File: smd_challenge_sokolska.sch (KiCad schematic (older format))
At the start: 13 parts, among them U01 usb_supply

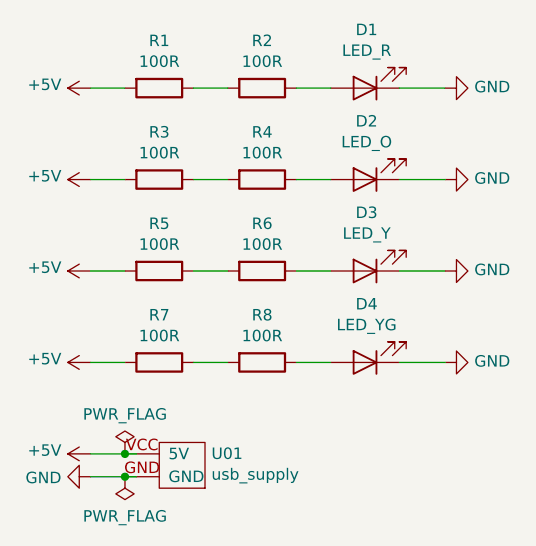
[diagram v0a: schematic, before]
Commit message: fixed part U01
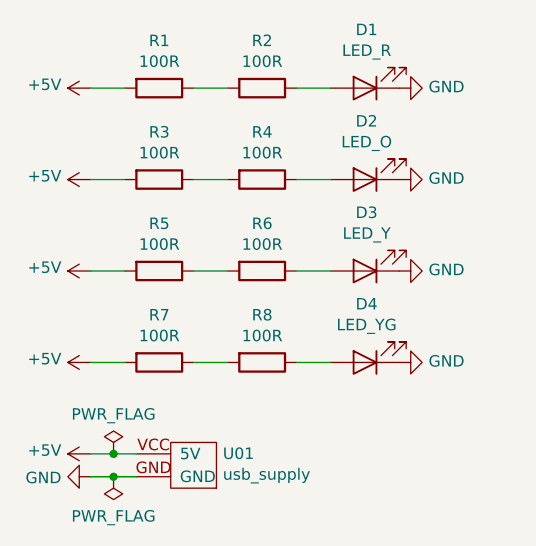
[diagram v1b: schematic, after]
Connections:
- wire segments 20 -> 16
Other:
- moved on the sheet: U01
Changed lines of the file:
@@
 Wire Wire Line
 	3350 3500 3500 3500
-$Comp
-L power:+5V #PWR01
-U 1 1 5FB98398
-P 2450 2300
-F 0 "#PWR01" H 2450 2150 50  0001 C CNN
-F 1 "+5V" V 2465 2428 50  0000 L CNN
-F 2 "" H 2450 2300 50  0001 C CNN
-F 3 "" H 2450 2300 50  0001 C CNN
-	1    2450 2300
-	0    -1   -1   0
-$EndComp
-$Comp
-L power:+5V #PWR03
-U 1 1 5FB98FA5
-P 2450 2700
-F 0 "#PWR03" H 2450 2550 50  0001 C CNN
-F 1 "+5V" V 2465 2828 50  0000 L CNN
-F 2 "" H 2450 2700 50  0001 C CNN
-F 3 "" H 2450 2700 50  0001 C CNN
-	1    2450 2700
-	0    -1   -1   0
-$EndComp
-$Comp
-L power:+5V #PWR05
-U 1 1 5FB993D5
-P 2450 3100
-F 0 "#PWR05" H 2450 2950 50  0001 C CNN
-F 1 "+5V" V 2465 3228 50  0000 L CNN
-F 2 "" H 2450 3100 50  0001 C CNN
-F 3 "" H 2450 3100 50  0001 C CNN
-	1    2450 3100
-	0    -1   -1   0
-$EndComp
-$Comp
-L power:+5V #PWR07
-U 1 1 5FB9982B
-P 2450 3500
-F 0 "#PWR07" H 2450 3350 50  0001 C CNN
-F 1 "+5V" V 2465 3628 50  0000 L CNN
-F 2 "" H 2450 3500 50  0001 C CNN
-F 3 "" H 2450 3500 50  0001 C CNN
-	1    2450 3500
-	0    -1   -1   0
-$EndComp
-$Comp
-L power:GND #PWR02
-U 1 1 5FB99BAF
-P 4000 2300
-F 0 "#PWR02" H 4000 2050 50  0001 C CNN
-F 1 "GND" V 4005 2172 50  0000 R CNN
-F 2 "" H 4000 2300 50  0001 C CNN
-F 3 "" H 4000 2300 50  0001 C CNN
-	1    4000 2300
-	0    -1   -1   0
-$EndComp
-$Comp
-L power:GND #PWR04
-U 1 1 5FB9A1E2
-P 4000 2700
-F 0 "#PWR04" H 4000 2450 50  0001 C CNN
-F 1 "GND" V 4005 2572 50  0000 R CNN
-F 2 "" H 4000 2700 50  0001 C CNN
-F 3 "" H 4000 2700 50  0001 C CNN
-	1    4000 2700
-	0    -1   -1   0
-$EndComp
-$Comp
-L power:GND #PWR06
-U 1 1 5FB9A544
-P 4000 3100
-F 0 "#PWR06" H 4000 2850 50  0001 C CNN
-F 1 "GND" V 4005 2972 50  0000 R CNN
-F 2 "" H 4000 3100 50  0001 C CNN
-F 3 "" H 4000 3100 50  0001 C CNN
-	1    4000 3100
-	0    -1   -1   0
-$EndComp
-$Comp
-L power:GND #PWR08
-U 1 1 5FB9A853
-P 4000 3500
-F 0 "#PWR08" H 4000 3250 50  0001 C CNN
-F 1 "GND" V 4005 3372 50  0000 R CNN
-F 2 "" H 4000 3500 50  0001 C CNN
-F 3 "" H 4000 3500 50  0001 C CNN
-	1    4000 3500
-	0    -1   -1   0
-$EndComp
 Wire Wire Line
 	2450 2300 2600 2300
@@
 Wire Wire Line
 	2450 3500 2600 3500
-Wire Wire Line
-	3800 3500 4000 3500
-Wire Wire Line
-	3800 3100 4000 3100
-Wire Wire Line
-	3800 2700 4000 2700
-Wire Wire Line
-	3800 2300 4000 2300
 $Comp
-L power:+5V #PWR09
-U 1 1 5FB9EA27
+L lib_smd_challenge:usb_supply U01
+U 1 1 5FBA6898
+P 2900 3950
+F 0 "U01" H 3028 4001 50  0000 L CNN
+F 1 "usb_supply" H 3028 3910 50  0000 L CNN
+F 2 "smd_challenge_sokolska:usb_supply" H 2700 4150 50  0001 C CNN
+F 3 "" H 2700 4150 50  0001 C CNN
+	1    2900 3950
+	1    0    0    -1
+$EndComp
+$Comp
+L power:+5V #PWR?
+U 1 1 5FBAC758
+P 2450 2300
+F 0 "#PWR?" H 2450 2150 50  0001 C CNN
+F 1 "+5V" V 2465 2428 50  0000 L CNN
+F 2 "" H 2450 2300 50  0001 C CNN
+F 3 "" H 2450 2300 50  0001 C CNN
+	1    2450 2300
+	0    -1   -1   0
+$EndComp
+$Comp
+L power:+5V #PWR?
+U 1 1 5FBACDBB
+P 2450 2700
+F 0 "#PWR?" H 2450 2550 50  0001 C CNN
+F 1 "+5V" V 2465 2828 50  0000 L CNN
+F 2 "" H 2450 2700 50  0001 C CNN
+F 3 "" H 2450 2700 50  0001 C CNN
+	1    2450 2700
+	0    -1   -1   0
+$EndComp
+$Comp
+L power:+5V #PWR?
+U 1 1 5FBAD238
+P 2450 3100
+F 0 "#PWR?" H 2450 2950 50  0001 C CNN
+F 1 "+5V" V 2465 3228 50  0000 L CNN
+F 2 "" H 2450 3100 50  0001 C CNN
+F 3 "" H 2450 3100 50  0001 C CNN
+	1    2450 3100
+	0    -1   -1   0
+$EndComp
+$Comp
+L power:+5V #PWR?
+U 1 1 5FBAD7C1
+P 2450 3500
+F 0 "#PWR?" H 2450 3350 50  0001 C CNN
+F 1 "+5V" V 2465 3628 50  0000 L CNN
+F 2 "" H 2450 3500 50  0001 C CNN
+F 3 "" H 2450 3500 50  0001 C CNN
+	1    2450 3500
+	0    -1   -1   0
+$EndComp
+$Comp
+L power:+5V #PWR?
+U 1 1 5FBADA85
 P 2450 3900
-F 0 "#PWR09" H 2450 3750 50  0001 C CNN
+F 0 "#PWR?" H 2450 3750 50  0001 C CNN
 F 1 "+5V" V 2465 4028 50  0000 L CNN
 F 2 "" H 2450 3900 50  0001 C CNN
@@
 $EndComp
 $Comp
-L power:GND #PWR010
-U 1 1 5FB9EDFF
+L power:GND #PWR?
+U 1 1 5FBAE10E
 P 2450 4000
-F 0 "#PWR010" H 2450 3750 50  0001 C CNN
+F 0 "#PWR?" H 2450 3750 50  0001 C CNN
 F 1 "GND" V 2455 3872 50  0000 R CNN
 F 2 "" H 2450 4000 50  0001 C CNN
@@
 	0    1    1    0
 $EndComp
+$Comp
+L power:GND #PWR?
+U 1 1 5FBAE6FF
+P 3800 2300
+F 0 "#PWR?" H 3800 2050 50  0001 C CNN
+F 1 "GND" V 3805 2172 50  0000 R CNN
+F 2 "" H 3800 2300 50  0001 C CNN
+F 3 "" H 3800 2300 50  0001 C CNN
+	1    3800 2300
+	0    -1   -1   0
+$EndComp
+$Comp
+L power:GND #PWR?
+U 1 1 5FBAFB2D
+P 3800 2700
+F 0 "#PWR?" H 3800 2450 50  0001 C CNN
+F 1 "GND" V 3805 2572 50  0000 R CNN
+F 2 "" H 3800 2700 50  0001 C CNN
+F 3 "" H 3800 2700 50  0001 C CNN
+	1    3800 2700
+	0    -1   -1   0
+$EndComp
+$Comp
+L power:GND #PWR?
+U 1 1 5FBAFEC9
+P 3800 3100
+F 0 "#PWR?" H 3800 2850 50  0001 C CNN
+F 1 "GND" V 3805 2972 50  0000 R CNN
+F 2 "" H 3800 3100 50  0001 C CNN
+F 3 "" H 3800 3100 50  0001 C CNN
+	1    3800 3100
+	0    -1   -1   0
+$EndComp
+$Comp
+L power:GND #PWR?
+U 1 1 5FBB0233
+P 3800 3500
+F 0 "#PWR?" H 3800 3250 50  0001 C CNN
+F 1 "GND" V 3805 3372 50  0000 R CNN
+F 2 "" H 3800 3500 50  0001 C CNN
+F 3 "" H 3800 3500 50  0001 C CNN
+	1    3800 3500
+	0    -1   -1   0
+$EndComp
 Wire Wire Line
-	2450 3900 2600 3900
+	2450 4000 2550 4000
 Wire Wire Line
-	2450 4000 2600 4000
+	2450 3900 2550 3900
 $Comp
-L power:PWR_FLAG #FLG01
-U 1 1 5FBA0533
-P 2600 3900
-F 0 "#FLG01" H 2600 3975 50  0001 C CNN
-F 1 "PWR_FLAG" H 2600 4073 50  0000 C CNN
-F 2 "" H 2600 3900 50  0001 C CNN
-F 3 "~" H 2600 3900 50  0001 C CNN
-	1    2600 3900
+L power:PWR_FLAG #FLG?
+U 1 1 5FBB0D33
+P 2550 3900
+F 0 "#FLG?" H 2550 3975 50  0001 C CNN
+F 1 "PWR_FLAG" H 2550 4073 50  0000 C CNN
+F 2 "" H 2550 3900 50  0001 C CNN
+F 3 "~" H 2550 3900 50  0001 C CNN
+	1    2550 3900
 	1    0    0    -1
 $EndComp
-Connection ~ 2600 3900
+Connection ~ 2550 3900
 Wire Wire Line
-	2600 3900 2650 3900
+	2550 3900 2650 3900
 $Comp
-L power:PWR_FLAG #FLG02
-U 1 1 5FBA0E1B
-P 2600 4000
-F 0 "#FLG02" H 2600 4075 50  0001 C CNN
-F 1 "PWR_FLAG" H 2600 4173 50  0000 C CNN
-F 2 "" H 2600 4000 50  0001 C CNN
-F 3 "~" H 2600 4000 50  0001 C CNN
-	1    2600 4000
+L power:PWR_FLAG #FLG?
+U 1 1 5FBB115E
+P 2550 4000
+F 0 "#FLG?" H 2550 4075 50  0001 C CNN
+F 1 "PWR_FLAG" H 2550 4173 50  0000 C CNN
+F 2 "" H 2550 4000 50  0001 C CNN
+F 3 "~" H 2550 4000 50  0001 C CNN
+	1    2550 4000
 	-1   0    0    1
 $EndComp
-Connection ~ 2600 4000
+Connection ~ 2550 4000
 Wire Wire Line
-	2600 4000 2650 4000
-$Comp
-L lib_smd_challenge:usb_supply U01
-U 1 1 5FBA6898
-P 2850 3950
-F 0 "U01" H 2978 4001 50  0000 L CNN
-F 1 "usb_supply" H 2978 3910 50  0000 L CNN
-F 2 "smd_challenge_sokolska:usb_supply" H 2650 4150 50  0001 C CNN
-F 3 "" H 2650 4150 50  0001 C CNN
-	1    2850 3950
-	1    0    0    -1
-$EndComp
+	2550 4000 2650 4000
 $EndSCHEMATC
